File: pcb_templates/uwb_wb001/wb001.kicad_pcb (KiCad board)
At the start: 2 copper layers, 40.1 x 22.2 mm, 2 parts, among them J101 Conn_01x01

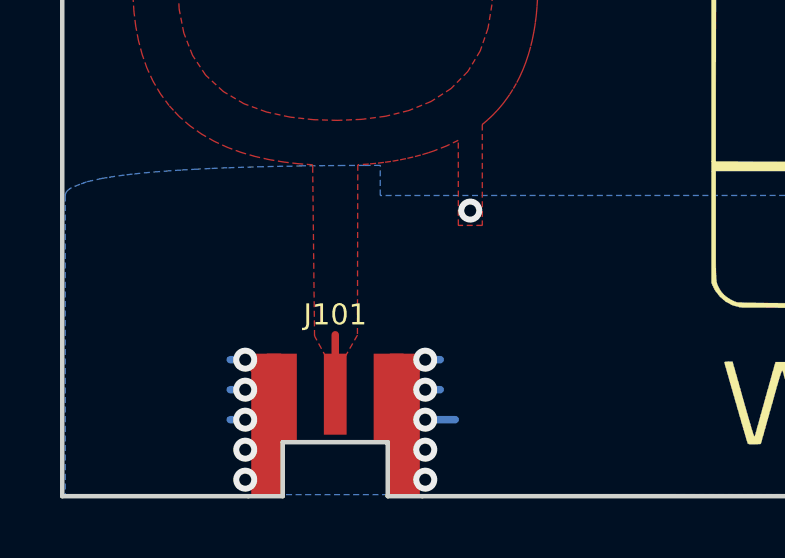
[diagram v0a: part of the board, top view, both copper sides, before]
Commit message: Fixed connections on antenna
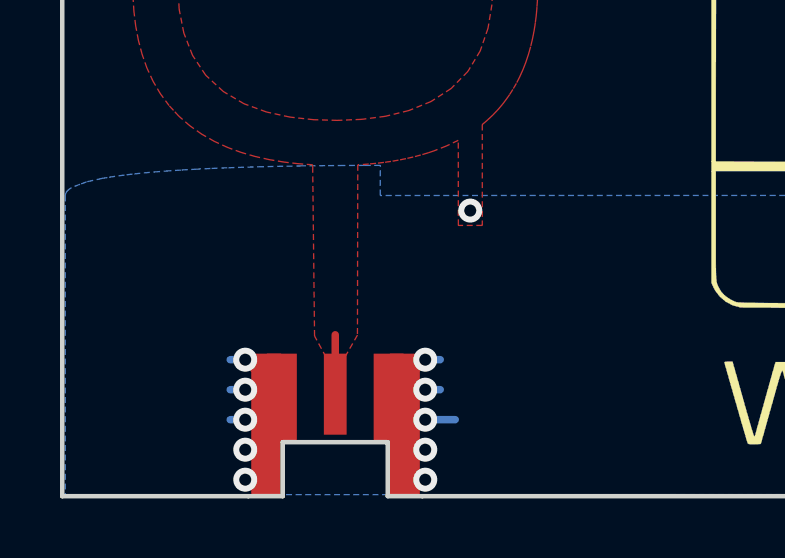
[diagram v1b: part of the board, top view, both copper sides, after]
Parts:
- J101: value Conn_01x01 -> MMCX, plug
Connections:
- J101 pad 1: Net-(AE101-Pad1) -> GND
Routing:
- net Net-(AE101-Pad1): track 1.98 -> 0.00 mm, vias 1 -> 0
- net GND: track 12.7 -> 14.7 mm, vias 10 -> 11
- added copper zone on F.Cu, net GND
- removed copper zone on F.Cu, net Net-(AE101-Pad1)
